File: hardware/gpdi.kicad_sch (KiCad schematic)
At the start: 12 parts, among them J5 GPDI_A, Q3 BSN20, U19 UCL0524P, U20 UCL0524P, U23 UCL0524P

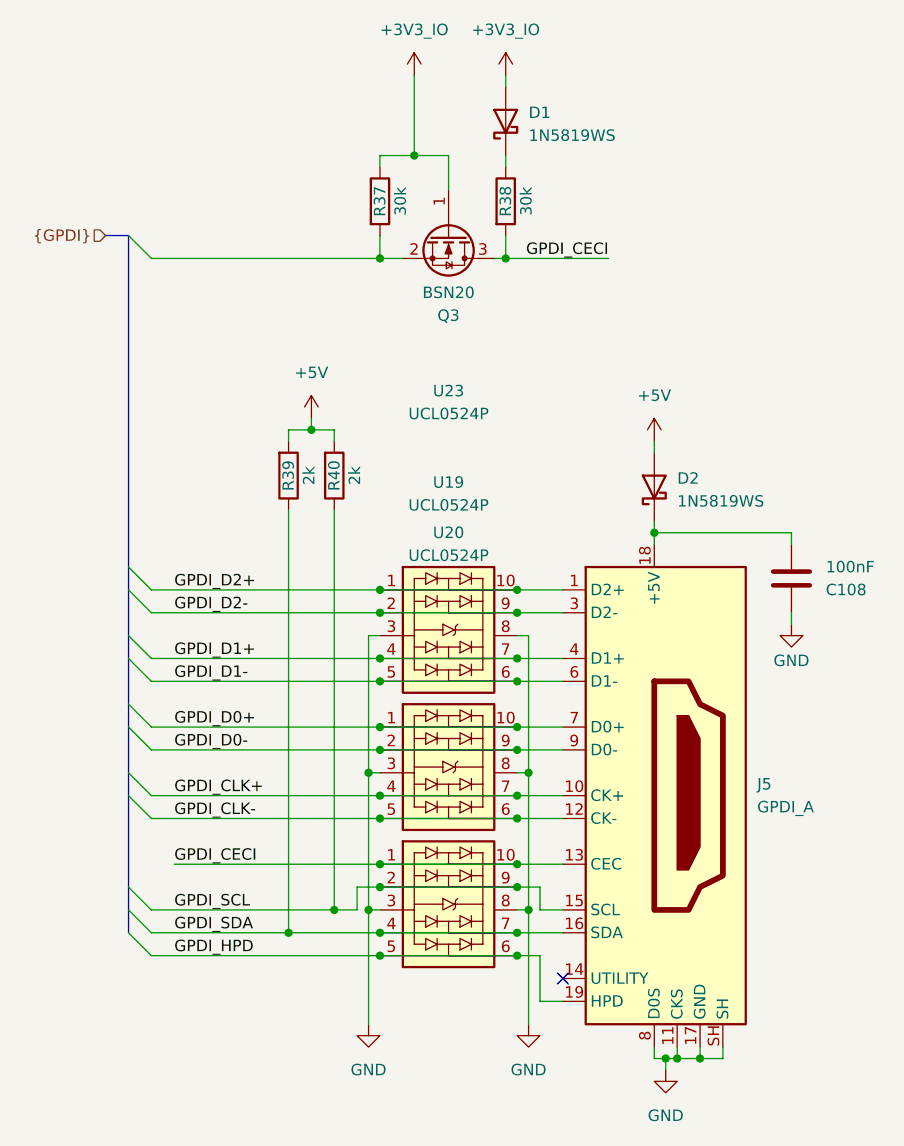
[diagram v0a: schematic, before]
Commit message: Update crystal
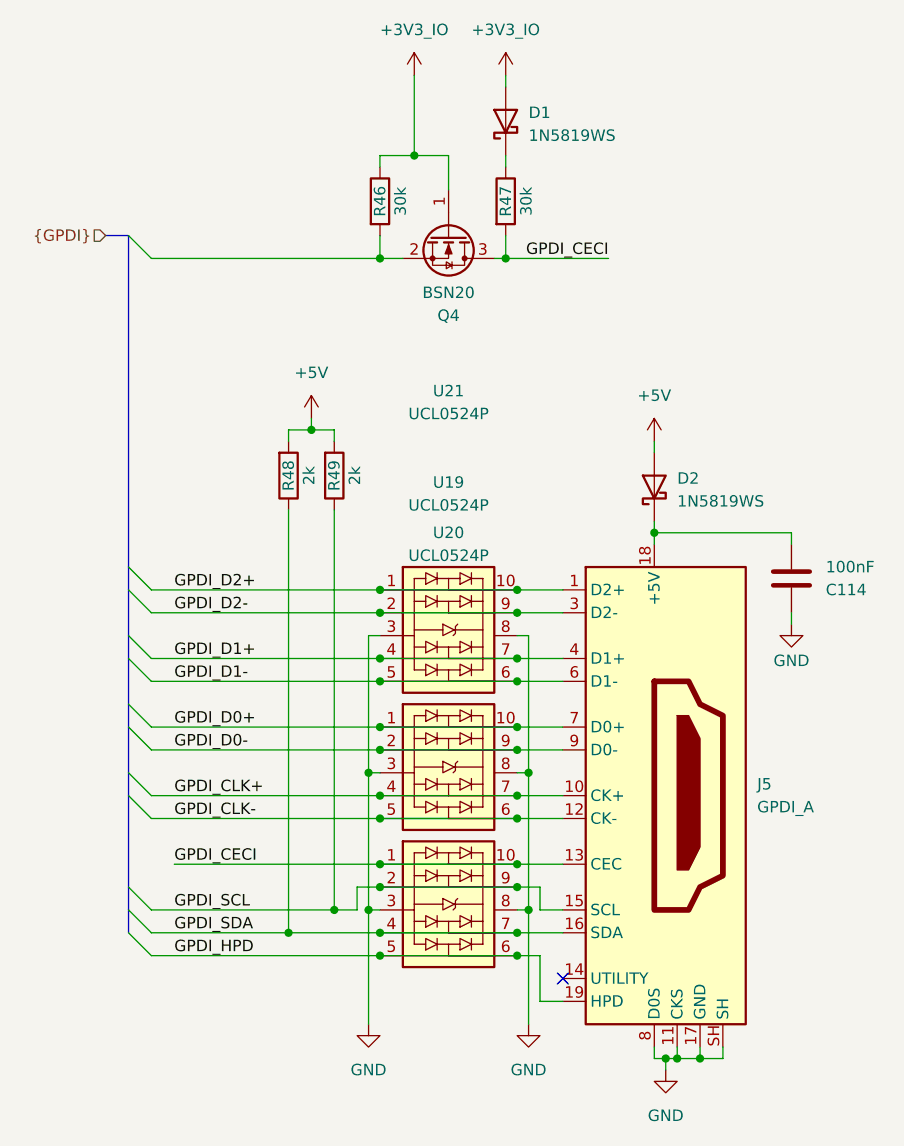
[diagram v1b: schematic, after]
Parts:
- renumbered C108 to C114, Q3 to Q4, R37 to R46, R38 to R47, R39 to R48, R40 to R49, U23 to U21
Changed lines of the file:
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@@
 		(on_board yes)
 		(dnp no)
-		(property "Reference" "R39"
+		(property "Reference" "R48"
 			(at 127 77.47 90)
 			(effects
@@
 			(project "cm0"
 				(path "/b53f5dbb-8078-4818-9e8f-fdf90ba6d854/f05ec484-f958-442a-a016-134b1e35dc2c"
-					(reference "R39")
+					(reference "R48")
 					(unit 1)
 				)
@@
 		(on_board yes)
 		(dnp no)
-		(property "Reference" "C108"
+		(property "Reference" "C114"
 			(at 186.69 90.1701 0)
 			(effects
@@
 			(project "cm0"
 				(path "/b53f5dbb-8078-4818-9e8f-fdf90ba6d854/f05ec484-f958-442a-a016-134b1e35dc2c"
-					(reference "C108")
+					(reference "C114")
 					(unit 1)
 				)
@@
 		(dnp no)
 		(fields_autoplaced yes)
-		(property "Reference" "#PWR0122"
+		(property "Reference" "#PWR0142"
 			(at 151.13 36.83 0)
 			(effects
@@
 			(project "cm0"
 				(path "/b53f5dbb-8078-4818-9e8f-fdf90ba6d854/f05ec484-f958-442a-a016-134b1e35dc2c"
-					(reference "#PWR0122")
+					(reference "#PWR0142")
 					(unit 1)
 				)
@@
 		(on_board yes)
 		(dnp no)
-		(property "Reference" "R38"
+		(property "Reference" "R47"
 			(at 151.13 46.99 90)
 			(effects
@@
 			(project "cm0"
 				(path "/b53f5dbb-8078-4818-9e8f-fdf90ba6d854/f05ec484-f958-442a-a016-134b1e35dc2c"
-					(reference "R38")
+					(reference "R47")
 					(unit 1)
 				)
@@
 		(on_board yes)
 		(dnp no)
-		(property "Reference" "Q3"
+		(property "Reference" "Q4"
 			(at 144.78 59.69 90)
 			(effects
@@
 			(project ""
 				(path "/b53f5dbb-8078-4818-9e8f-fdf90ba6d854/f05ec484-f958-442a-a016-134b1e35dc2c"
-					(reference "Q3")
+					(reference "Q4")
 					(unit 1)
 				)
@@
 		(dnp no)
 		(fields_autoplaced yes)
-		(property "Reference" "#PWR0127"
+		(property "Reference" "#PWR0147"
 			(at 153.67 144.78 0)
 			(effects
@@
 			(project ""
 				(path "/b53f5dbb-8078-4818-9e8f-fdf90ba6d854/f05ec484-f958-442a-a016-134b1e35dc2c"
-					(reference "#PWR0127")
+					(reference "#PWR0147")
 					(unit 1)
 				)
@@
 		(dnp no)
 		(fields_autoplaced yes)
-		(property "Reference" "#PWR0126"
+		(property "Reference" "#PWR0146"
 			(at 135.89 144.78 0)
 			(effects
@@
 			(project "cm0"
 				(path "/b53f5dbb-8078-4818-9e8f-fdf90ba6d854/f05ec484-f958-442a-a016-134b1e35dc2c"
-					(reference "#PWR0126")
+					(reference "#PWR0146")
 					(unit 1)
 				)
@@
 		(on_board yes)
 		(dnp no)
-		(property "Reference" "#PWR0125"
+		(property "Reference" "#PWR0145"
 			(at 182.88 100.33 0)
 			(effects
@@
 			(project "cm0"
 				(path "/b53f5dbb-8078-4818-9e8f-fdf90ba6d854/f05ec484-f958-442a-a016-134b1e35dc2c"
-					(reference "#PWR0125")
+					(reference "#PWR0145")
 					(unit 1)
 				)
@@
 		(dnp no)
 		(fields_autoplaced yes)
-		(property "Reference" "#PWR0128"
+		(property "Reference" "#PWR0148"
 			(at 168.91 149.86 0)
 			(effects
@@
 			(project ""
 				(path "/b53f5dbb-8078-4818-9e8f-fdf90ba6d854/f05ec484-f958-442a-a016-134b1e35dc2c"
-					(reference "#PWR0128")
+					(reference "#PWR0148")
 					(unit 1)
 				)
@@
 		(on_board yes)
 		(dnp no)
-		(property "Reference" "R40"
+		(property "Reference" "R49"
 			(at 132.08 77.47 90)
 			(effects
@@
 			(project "cm0"
 				(path "/b53f5dbb-8078-4818-9e8f-fdf90ba6d854/f05ec484-f958-442a-a016-134b1e35dc2c"
-					(reference "R40")
+					(reference "R49")
 					(unit 1)
 				)
@@
 		(dnp no)
 		(fields_autoplaced yes)
-		(property "Reference" "#PWR0124"
+		(property "Reference" "#PWR0144"
 			(at 167.64 77.47 0)
 			(effects
@@
 			(project ""
 				(path "/b53f5dbb-8078-4818-9e8f-fdf90ba6d854/f05ec484-f958-442a-a016-134b1e35dc2c"
-					(reference "#PWR0124")
+					(reference "#PWR0144")
 					(unit 1)
 				)
@@
 		(on_board yes)
 		(dnp no)
-		(property "Reference" "U23"
+		(property "Reference" "U21"
 			(at 144.78 68.072 0)
 			(effects
@@
 			(project "cm0"
 				(path "/b53f5dbb-8078-4818-9e8f-fdf90ba6d854/f05ec484-f958-442a-a016-134b1e35dc2c"
-					(reference "U23")
+					(reference "U21")
 					(unit 1)
 				)
@@
 		(dnp no)
 		(fields_autoplaced yes)
-		(property "Reference" "#PWR0123"
+		(property "Reference" "#PWR0143"
 			(at 129.54 74.93 0)
 			(effects
@@
 			(project "cm0"
 				(path "/b53f5dbb-8078-4818-9e8f-fdf90ba6d854/f05ec484-f958-442a-a016-134b1e35dc2c"
-					(reference "#PWR0123")
+					(reference "#PWR0143")
 					(unit 1)
 				)
@@
 		(dnp no)
 		(fields_autoplaced yes)
-		(property "Reference" "#PWR0121"
+		(property "Reference" "#PWR0141"
 			(at 140.97 36.83 0)
 			(effects
@@
 			(project ""
 				(path "/b53f5dbb-8078-4818-9e8f-fdf90ba6d854/f05ec484-f958-442a-a016-134b1e35dc2c"
-					(reference "#PWR0121")
+					(reference "#PWR0141")
 					(unit 1)
 				)
@@
 		(on_board yes)
 		(dnp no)
-		(property "Reference" "R37"
+		(property "Reference" "R46"
 			(at 137.16 46.99 90)
 			(effects
@@
 			(project "cm0"
 				(path "/b53f5dbb-8078-4818-9e8f-fdf90ba6d854/f05ec484-f958-442a-a016-134b1e35dc2c"
-					(reference "R37")
-					(unit 1)
-				)
+					(reference "R46")
+					(unit 1)
+				)

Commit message: Add schematic pdf
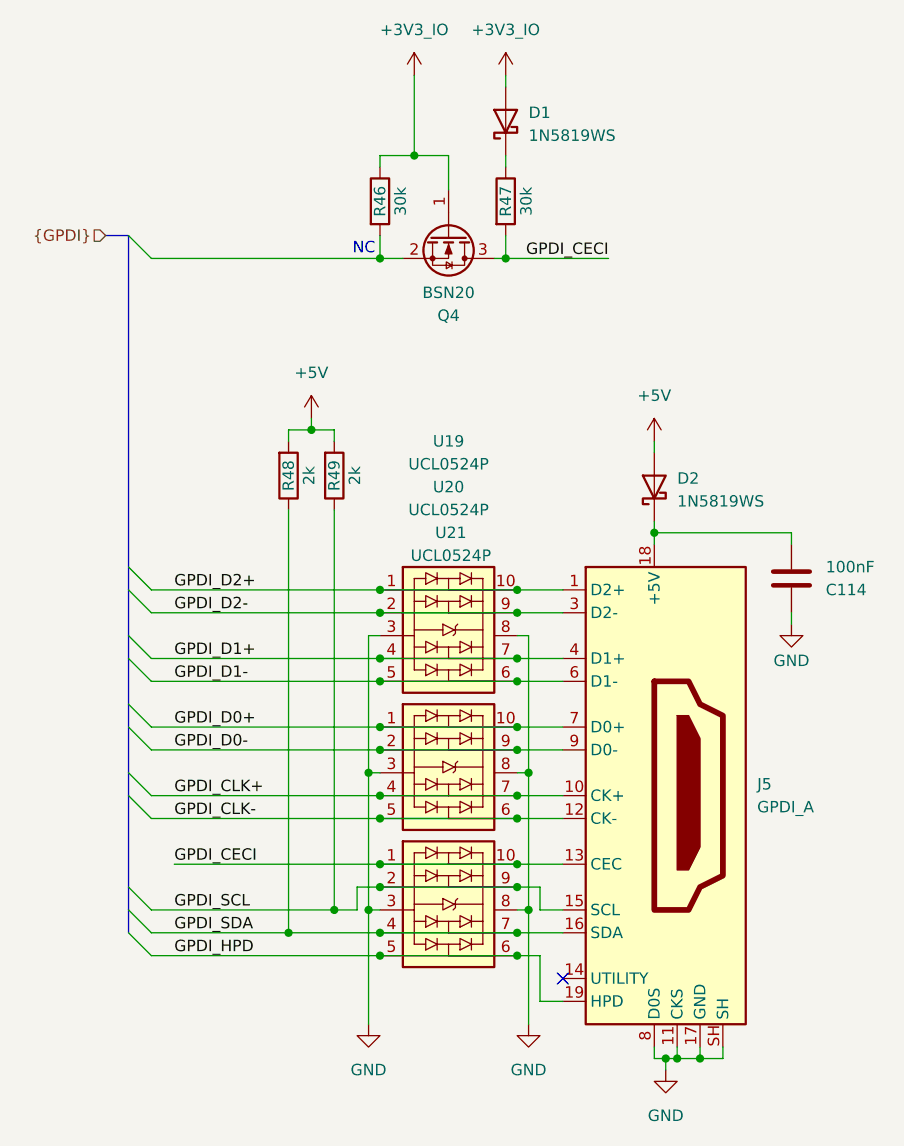
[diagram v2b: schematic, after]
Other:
- note added: "NC"
- title: Icepi CM0 -> Icepi SBC
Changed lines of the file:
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@@
 	(paper "A4")
 	(title_block
-		(title "Icepi CM0")
-		(date "2025-11-21")
+		(title "Icepi SBC")
+		(date "2025-12-21")
 		(rev "v1.0")
 		(company "Icy Electronics")
 		(comment 1 "Chengyin Yao (cheyao)")
-		(comment 2 "https://github.com/cheyao/icepi-cm0")
+		(comment 2 "https://github.com/cheyao/icepi-sbc")
 		(comment 3 "License: Solderpad")
 	)
@@
 		)
 	)
+	(text "NC"
+		(exclude_from_sim no)
+		(at 135.382 52.324 0)
+		(effects
+			(font
+				(size 1.27 1.27)
+				(color 255 153 0 1)
+			)
+		)
+	)
 	(junction
 		(at 137.16 113.03)
@@
 		(dnp no)
 		(property "Reference" "U19"
-			(at 144.78 78.232 0)
+			(at 144.78 73.66 0)
 			(effects
 				(font
@@
 		)
 		(property "Value" "UCL0524P"
-			(at 144.78 80.772 0)
+			(at 144.78 76.2 0)
 			(effects
 				(font
@@
 		(dnp no)
 		(property "Reference" "U20"
-			(at 144.78 83.82 0)
+			(at 144.78 78.74 0)
 			(effects
 				(font
@@
 		)
 		(property "Value" "UCL0524P"
-			(at 144.78 86.36 0)
+			(at 144.78 81.28 0)
 			(effects
 				(font
@@
 		(dnp no)
 		(property "Reference" "U21"
-			(at 144.78 68.072 0)
+			(at 145.034 83.82 0)
 			(effects
 				(font
@@
 		)
 		(property "Value" "UCL0524P"
-			(at 144.78 70.612 0)
+			(at 145.034 86.36 0)
 			(effects
 				(font
